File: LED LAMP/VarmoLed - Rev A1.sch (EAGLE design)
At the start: 20 parts, among them J1 22-05-7038-03, U1 IRLML6344TRPBF

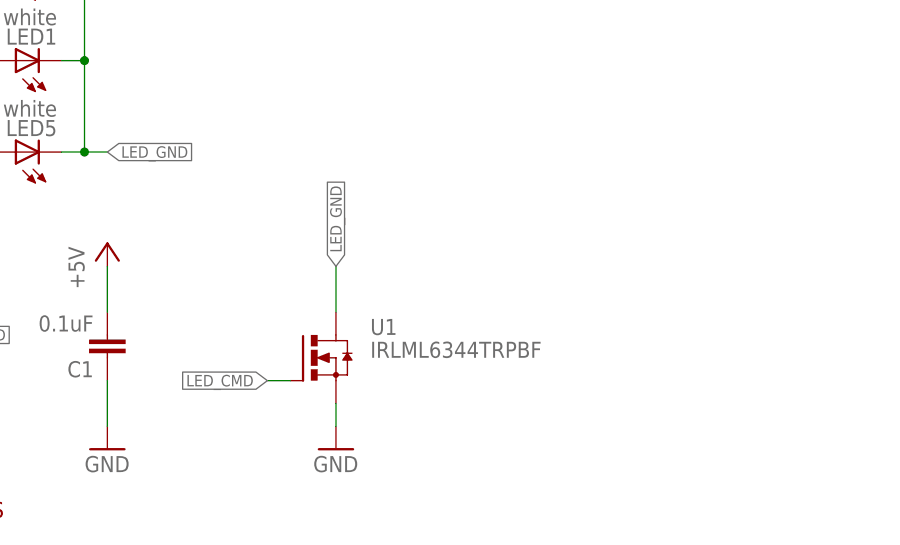
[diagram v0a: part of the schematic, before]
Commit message: Rename Varmo LED to lamp LED and add a resitor on input of the transistor
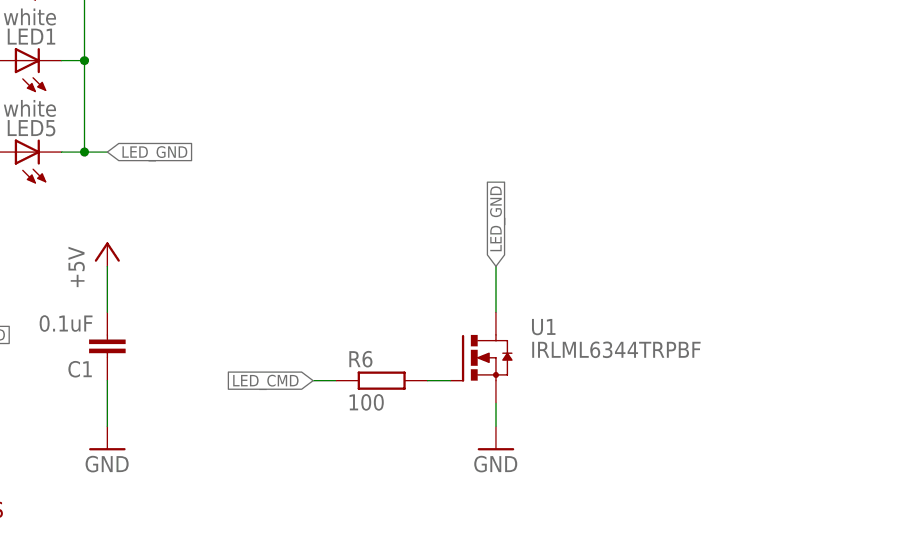
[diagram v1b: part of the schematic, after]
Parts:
- added R6: 100, rcl:R-EU_R0603
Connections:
- new net N$6: R6.2, U1.G
- net LED_CMD: now also R6.1; no longer U1.G
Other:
- moved on the sheet: U1
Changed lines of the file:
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@@
 <part name="U1" library="International_Rectifier_By_element14_Batch_1" deviceset="IRLML6344TRPBF" device=""/>
 <part name="GND4" library="supply1" deviceset="GND" device=""/>
+<part name="R6" library="rcl" deviceset="R-EU_" device="R0603" value="100"/>
 </parts>
 <sheets>
@@
 <instance part="JP4" gate="G$1" x="376.174" y="31.75"/>
 <instance part="J1" gate="-3" x="33.02" y="43.18" rot="R180"/>
-<instance part="U1" gate="A" x="86.36" y="40.64"/>
-<instance part="GND4" gate="1" x="86.36" y="30.48"/>
+<instance part="U1" gate="A" x="104.14" y="40.64"/>
+<instance part="GND4" gate="1" x="104.14" y="30.48"/>
+<instance part="R6" gate="G$1" x="91.44" y="38.1"/>
 </instances>
 <busses>
@@
 <pinref part="U1" gate="A" pin="S"/>
 <pinref part="GND4" gate="1" pin="GND"/>
-<wire x1="86.36" y1="33.02" x2="86.36" y2="35.56" width="0.1524" layer="91"/>
+<wire x1="104.14" y1="33.02" x2="104.14" y2="35.56" width="0.1524" layer="91"/>
 </segment>
 </net>
@@
 </segment>
 <segment>
-<pinref part="U1" gate="A" pin="G"/>
-<wire x1="81.28" y1="38.1" x2="78.74" y2="38.1" width="0.1524" layer="91"/>
-<label x="78.74" y="38.1" size="1.27" layer="95" rot="R180" xref="yes"/>
+<label x="83.82" y="38.1" size="1.27" layer="95" rot="R180" xref="yes"/>
+<pinref part="R6" gate="G$1" pin="1"/>
+<wire x1="86.36" y1="38.1" x2="83.82" y2="38.1" width="0.1524" layer="91"/>
 </segment>
 </net>
@@
 <segment>
 <pinref part="U1" gate="A" pin="D"/>
-<wire x1="86.36" y1="45.72" x2="86.36" y2="50.8" width="0.1524" layer="91"/>
-<label x="86.36" y="50.8" size="1.27" layer="95" rot="R90" xref="yes"/>
+<wire x1="104.14" y1="45.72" x2="104.14" y2="50.8" width="0.1524" layer="91"/>
+<label x="104.14" y="50.8" size="1.27" layer="95" rot="R90" xref="yes"/>
 </segment>
 <segment>
@@
 </segment>
 </net>
+<net name="N$6" class="0">
+<segment>
+<pinref part="R6" gate="G$1" pin="2"/>
+<pinref part="U1" gate="A" pin="G"/>
+<wire x1="96.52" y1="38.1" x2="99.06" y2="38.1" width="0.1524" layer="91"/>
+</segment>
+</net>
